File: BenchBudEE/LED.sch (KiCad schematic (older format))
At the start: 0 parts

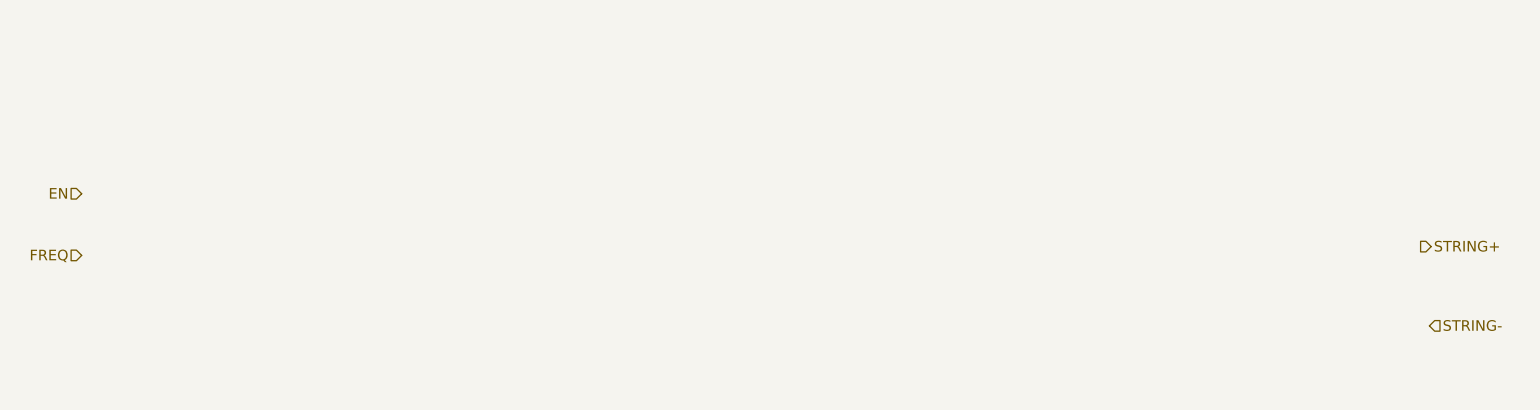
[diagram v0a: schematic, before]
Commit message: LED driver schematic
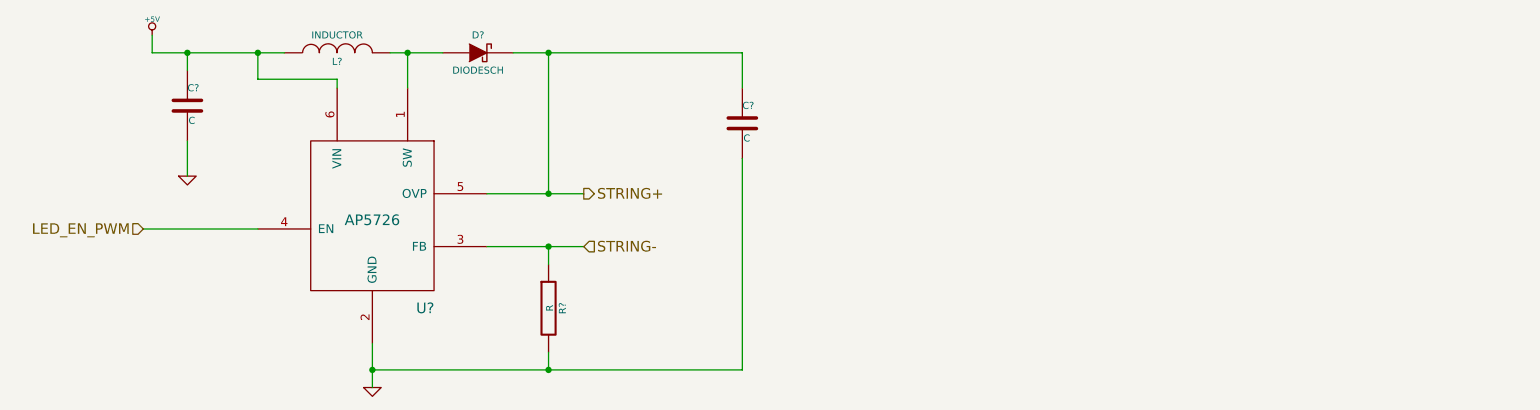
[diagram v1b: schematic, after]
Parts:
- added C? (x2): C, ~, symbol C
- added D?: DIODESCH, ~, symbol DIODESCH
- added L?: INDUCTOR, ~, symbol INDUCTOR
- added R?: R, ~, symbol R
- added U?: AP5726, symbol AP5726
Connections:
- net STRING+: now also C?.1, D?.2 (K), U?.5 (OVP)
- net STRING-: now also R?.1, U?.3 (FB)
- new net: D?.1 (A), L?.2, U?.1 (SW)
- new net +5V: C?.1, L?.1, U?.6 (VIN)
- new net GND: C?.2, C?.2, R?.2, U?.2 (GND)
- new net LED_EN_PWM: U?.4 (EN)
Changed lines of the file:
@@
 Sheet 4 9
 Title ""
-Date "13 feb 2014"
+Date "16 feb 2014"
 Rev ""
 Comp ""
@@
 Comment4 ""
 $EndDescr
-Text HLabel 1650 2500 0    60   Input ~ 0
-EN
-Text HLabel 1650 2850 0    60   Input ~ 0
-FREQ
-Text HLabel 9250 2800 2    60   Output ~ 0
+Text HLabel 2000 2700 0    60   Input ~ 0
+LED_EN_PWM
+Text HLabel 4500 2500 2    60   Output ~ 0
 STRING+
-Text HLabel 9300 3250 2    60   Input ~ 0
+Text HLabel 4500 2800 2    60   Input ~ 0
 STRING-
+$Comp
+L AP5726 U?
+U 1 1 5300301C
+P 3300 2500
+F 0 "U?" H 3600 1850 60  0000 C CNN
+F 1 "AP5726" H 3300 2350 60  0000 C CNN
+F 2 "" H 3300 2500 60  0000 C CNN
+F 3 "" H 3300 2500 60  0000 C CNN
+	1    3300 2500
+	1    0    0    -1
+$EndComp
+Wire Wire Line
+	2000 2700 2650 2700
+$Comp
+L +5V #PWR?
+U 1 1 53003233
+P 2050 1600
+F 0 "#PWR?" H 2050 1690 20  0001 C CNN
+F 1 "+5V" H 2050 1690 30  0000 C CNN
+F 2 "" H 2050 1600 60  0000 C CNN
+F 3 "" H 2050 1600 60  0000 C CNN
+	1    2050 1600
+	1    0    0    -1
+$EndComp
+$Comp
+L GND #PWR?
+U 1 1 53003244
+P 3300 3600
+F 0 "#PWR?" H 3300 3600 30  0001 C CNN
+F 1 "GND" H 3300 3530 30  0001 C CNN
+F 2 "" H 3300 3600 60  0000 C CNN
+F 3 "" H 3300 3600 60  0000 C CNN
+	1    3300 3600
+	1    0    0    -1
+$EndComp
+Wire Wire Line
+	3300 3600 3300 3350
+$Comp
+L C C?
+U 1 1 5300357D
+P 2250 2000
+F 0 "C?" H 2250 2100 40  0000 L CNN
+F 1 "C" H 2256 1915 40  0000 L CNN
+F 2 "~" H 2288 1850 30  0000 C CNN
+F 3 "~" H 2250 2000 60  0000 C CNN
+	1    2250 2000
+	1    0    0    -1
+$EndComp
+$Comp
+L GND #PWR?
+U 1 1 5300358C
+P 2250 2400
+F 0 "#PWR?" H 2250 2400 30  0001 C CNN
+F 1 "GND" H 2250 2330 30  0001 C CNN
+F 2 "" H 2250 2400 60  0000 C CNN
+F 3 "" H 2250 2400 60  0000 C CNN
+	1    2250 2400
+	1    0    0    -1
+$EndComp
+Wire Wire Line
+	2250 2400 2250 2200
+Wire Wire Line
+	2250 1800 2250 1700
+Wire Wire Line
+	2050 1700 2800 1700
+Wire Wire Line
+	2050 1700 2050 1600
+$Comp
+L INDUCTOR L?
+U 1 1 530035A4
+P 3100 1700
+F 0 "L?" V 3050 1700 40  0000 C CNN
+F 1 "INDUCTOR" V 3200 1700 40  0000 C CNN
+F 2 "~" H 3100 1700 60  0000 C CNN
+F 3 "~" H 3100 1700 60  0000 C CNN
+	1    3100 1700
+	0    -1   -1   0
+$EndComp
+Connection ~ 2250 1700
+Wire Wire Line
+	2650 1700 2650 1850
+Wire Wire Line
+	2650 1850 3100 1850
+Wire Wire Line
+	3100 1850 3100 1900
+Connection ~ 2650 1700
+Wire Wire Line
+	3400 1700 3700 1700
+Wire Wire Line
+	3500 1700 3500 1900
+$Comp
+L DIODESCH D?
+U 1 1 530035EA
+P 3900 1700
+F 0 "D?" H 3900 1800 40  0000 C CNN
+F 1 "DIODESCH" H 3900 1600 40  0000 C CNN
+F 2 "~" H 3900 1700 60  0000 C CNN
+F 3 "~" H 3900 1700 60  0000 C CNN
+	1    3900 1700
+	1    0    0    -1
+$EndComp
+Connection ~ 3500 1700
+$Comp
+L C C?
+U 1 1 53003611
+P 5400 2100
+F 0 "C?" H 5400 2200 40  0000 L CNN
+F 1 "C" H 5406 2015 40  0000 L CNN
+F 2 "~" H 5438 1950 30  0000 C CNN
+F 3 "~" H 5400 2100 60  0000 C CNN
+	1    5400 2100
+	1    0    0    -1
+$EndComp
+Wire Wire Line
+	5400 1900 5400 1700
+Wire Wire Line
+	5400 1700 4100 1700
+Wire Wire Line
+	3300 3500 5400 3500
+Wire Wire Line
+	5400 3500 5400 2300
+Wire Wire Line
+	3950 2500 4500 2500
+Wire Wire Line
+	4300 2500 4300 1700
+Connection ~ 4300 1700
+Connection ~ 4300 2500
+Wire Wire Line
+	4500 2800 3950 2800
+$Comp
+L R R?
+U 1 1 53003684
+P 4300 3150
+F 0 "R?" V 4380 3150 40  0000 C CNN
+F 1 "R" V 4307 3151 40  0000 C CNN
+F 2 "~" V 4230 3150 30  0000 C CNN
+F 3 "~" H 4300 3150 30  0000 C CNN
+	1    4300 3150
+	1    0    0    -1
+$EndComp
+Wire Wire Line
+	4300 2900 4300 2800
+Connection ~ 4300 2800
+Wire Wire Line
+	4300 3400 4300 3500
+Connection ~ 4300 3500
+Connection ~ 3300 3500
 $EndSCHEMATC

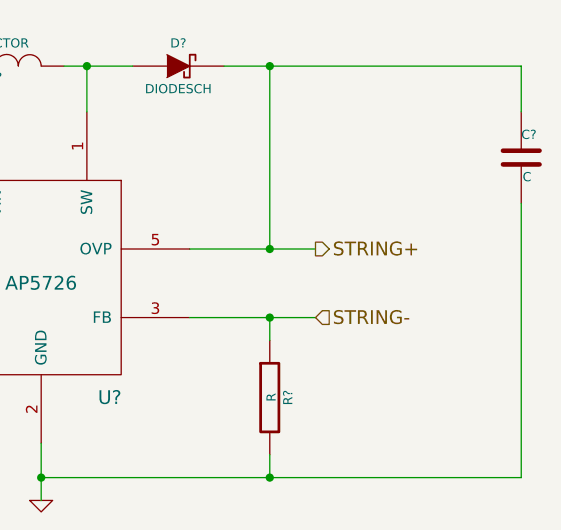
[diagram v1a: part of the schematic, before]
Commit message: arduino schematic and interconnection
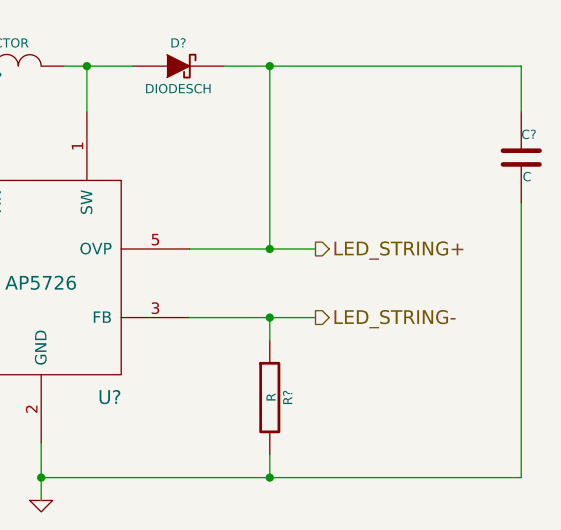
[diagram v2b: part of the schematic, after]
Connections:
- net STRING+ renamed LED_STRING+
- net STRING- renamed LED_STRING-
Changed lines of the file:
@@
 Sheet 4 9
 Title ""
-Date "16 feb 2014"
+Date "17 feb 2014"
 Rev ""
 Comp ""
@@
 LED_EN_PWM
 Text HLabel 4500 2500 2    60   Output ~ 0
-STRING+
-Text HLabel 4500 2800 2    60   Input ~ 0
-STRING-
+LED_STRING+
+Text HLabel 4500 2800 2    60   Output ~ 0
+LED_STRING-
 $Comp
 L AP5726 U?
